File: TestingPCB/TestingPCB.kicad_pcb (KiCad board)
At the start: 2 copper layers, 15 parts, among them J1 Conn_01x04, J2 USB_C_Receptacle_USB2.0_14P, J3 Conn_01x08, U1 SC0915, U2 CP2102N-Axx-xQFN24, U3 USBLC6-2P6

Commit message: v1 of PCB
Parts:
- added H1: MountingHole, MountingHole:MountingHole_3.2mm_M3_ISO7380_Pad_TopBottom, F.Cu at (95.0, 70.0)
- added H2: MountingHole, MountingHole:MountingHole_3.2mm_M3_ISO7380_Pad_TopBottom, F.Cu at (175.0, 70.0)
- added H3: MountingHole, MountingHole:MountingHole_3.2mm_M3_ISO7380_Pad_TopBottom, F.Cu at (95.0, 140.0)
- added H4: MountingHole, MountingHole:MountingHole_3.2mm_M3_ISO7380_Pad_TopBottom, F.Cu at (175.0, 140.0)
- moved J3 132.0 mm to (135.0, 137.5), turned to -90 degrees
- moved J1 112.0 mm to (160.0, 72.5), turned to 90 degrees
- moved R3 92.8 mm to (108.0, 113.5), turned to 90 degrees
- moved R4 87.4 mm to (103.0, 113.5), turned to -90 degrees
- moved C1 86.2 mm to (104.5, 104.5), turned to -90 degrees
- moved C2 84.7 mm to (107.5, 104.5), turned to -90 degrees
- moved R5 82.0 mm to (111.5, 104.5), turned to 90 degrees
- moved R1 78.5 mm to (116.0, 82.5), turned to 90 degrees
- moved C3 74.0 mm to (99.5, 100.0), turned to 180 degrees
- moved U2 70.3 mm to (108.2, 98.6)
- moved C4 68.8 mm to (99.5, 97.5), turned to 180 degrees
- moved R2 67.5 mm to (103.5, 82.5), turned to 90 degrees
- moved U1 65.3 mm to (135.0, 92.5)
- moved U3 63.1 mm to (109.5, 82.3), turned to -90 degrees
- moved J2 49.5 mm to (110.0, 69.5), turned to 180 degrees
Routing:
- net /3.3V: track 0.00 -> 111.3 mm, vias 0 -> 3
- net /USB 5V: track 0.00 -> 75.9 mm, vias 0 -> 6
- net /D7: track 0.00 -> 63.3 mm, vias 0 -> 2
- net /D6: track 0.00 -> 55.1 mm, vias 0 -> 2
- net /D5: track 0.00 -> 50.8 mm, vias 0 -> 2
- net /D4: track 0.00 -> 45.8 mm, vias 0 -> 2
- net /D3: track 0.00 -> 41.6 mm, vias 0 -> 2
- net /RX: track 0.00 -> 37.5 mm, vias 0 -> 2
- net /D2: track 0.00 -> 36.7 mm, vias 0 -> 2
- net /TX: track 0.00 -> 36.0 mm
- net /5V: track 0.00 -> 32.3 mm
- net /D1: track 0.00 -> 30.9 mm, vias 0 -> 2
- net /D0: track 0.00 -> 27.1 mm
- net /D_N: track 0.00 -> 21.9 mm, vias 0 -> 2
- net /D_P: track 0.00 -> 18.5 mm
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- added copper zone on B.Cu, net /GND
- added copper zone on F.Cu, net /GND
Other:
- board outline added: 90 x 80 mm
- board text added: "5V"
- board text added: "ARM vs RISC-V Thesis Board"
- board text added: "By Robbie Leslie"
- board text added: "D0"
- board text added: "D1"
- board text added: "D2"
- board text added: "D3"
- board text added: "D4"
- board text added: "D5"
- board text added: "D6"
- board text added: "D7"
- board text added: "GND"
- board text added: "Lafayette College Electrical and Computer Engineering"
- board text added: "v1.0"

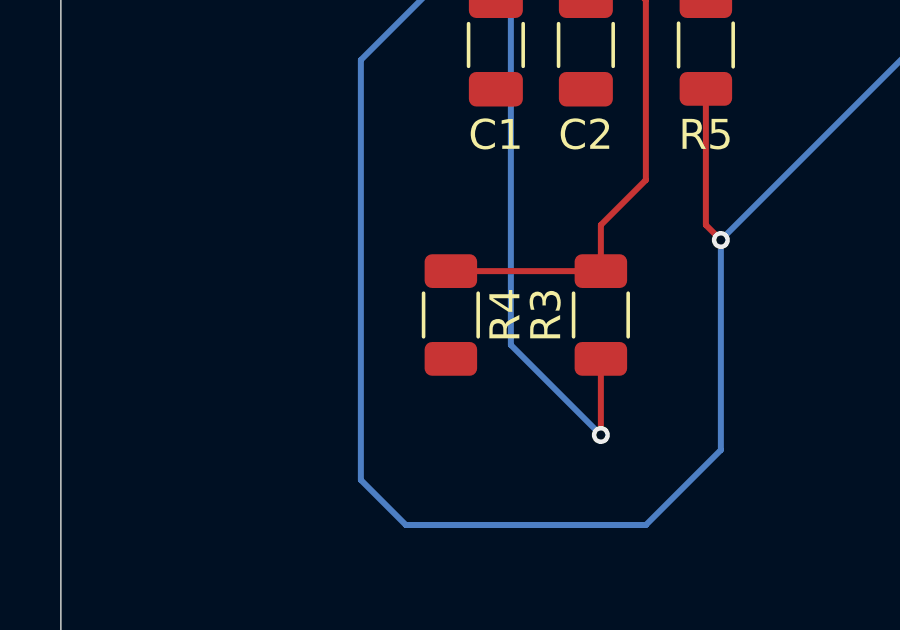
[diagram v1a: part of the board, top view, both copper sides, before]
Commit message: Updated silkscreen
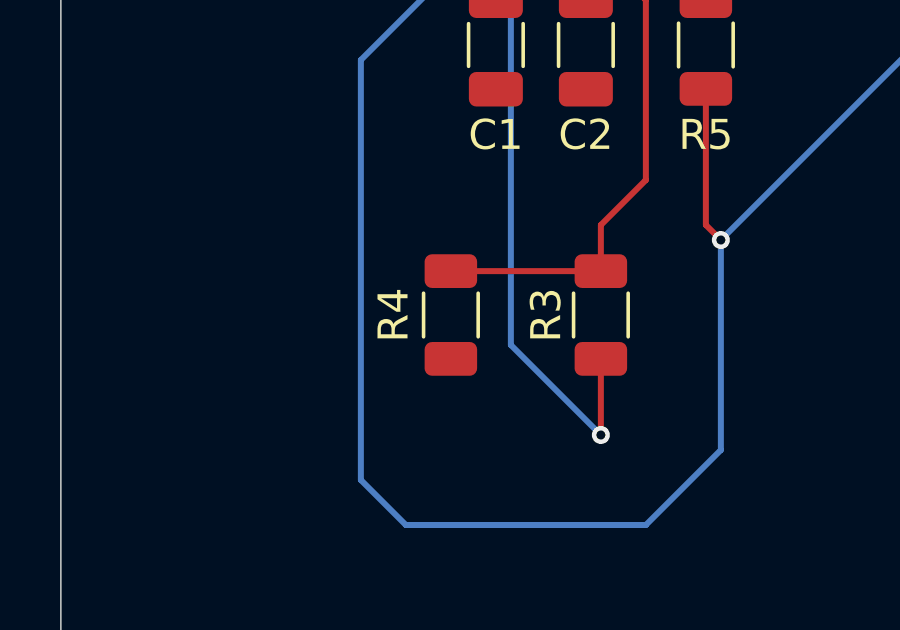
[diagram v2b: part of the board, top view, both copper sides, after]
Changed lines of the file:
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@@
 			(size 3.6 3.6)
 			(drill 3.2)
-			(layers "*.Cu" "*.Mask")
+			(layers "*.Cu" "*.Mask" "In1.Cu" "In2.Cu" "In3.Cu" "In4.Cu" "In5.Cu" "In6.Cu"
+				"In7.Cu" "In8.Cu" "In9.Cu" "In10.Cu" "In11.Cu" "In12.Cu" "In13.Cu" "In14.Cu"
+				"In15.Cu" "In16.Cu" "In17.Cu" "In18.Cu" "In19.Cu" "In20.Cu" "In21.Cu"
+				"In22.Cu" "In23.Cu" "In24.Cu" "In25.Cu" "In26.Cu" "In27.Cu" "In28.Cu"
+				"In29.Cu" "In30.Cu"
+			)
 			(remove_unused_layers no)
 		)
@@
 			(size 3.6 3.6)
 			(drill 3.2)
-			(layers "*.Cu" "*.Mask")
+			(layers "*.Cu" "*.Mask" "In1.Cu" "In2.Cu" "In3.Cu" "In4.Cu" "In5.Cu" "In6.Cu"
+				"In7.Cu" "In8.Cu" "In9.Cu" "In10.Cu" "In11.Cu" "In12.Cu" "In13.Cu" "In14.Cu"
+				"In15.Cu" "In16.Cu" "In17.Cu" "In18.Cu" "In19.Cu" "In20.Cu" "In21.Cu"
+				"In22.Cu" "In23.Cu" "In24.Cu" "In25.Cu" "In26.Cu" "In27.Cu" "In28.Cu"
+				"In29.Cu" "In30.Cu"
+			)
 			(remove_unused_layers no)
 		)
@@
 		(tags "resistor")
 		(property "Reference" "R4"
-			(at 0 -1.82 90)
+			(at 0 1.908 90)
 			(layer "F.SilkS")
 			(effects
@@
 		)
 		(fp_text user "${REFERENCE}"
-			(at -0.48 0 360)
+			(at -0.48 0 0)
 			(layer "F.Fab")
 			(effects
@@
 		(tags "capacitor")
 		(property "Reference" "C3"
-			(at 3.5 0 360)
+			(at 3.5 0 0)
 			(layer "F.SilkS")
 			(effects
@@
 		)
 		(property "Value" "4.7uF"
-			(at 0 1.85 360)
+			(at 0 1.85 0)
 			(layer "F.Fab")
 			(effects
@@
 		)
 		(fp_text user "${REFERENCE}"
-			(at 0 0 360)
+			(at 0 0 0)
 			(layer "F.Fab")
 			(effects
@@
 		)
 		(fp_text user "${REFERENCE}"
-			(at -0.48 0 360)
+			(at -0.48 0 0)
 			(layer "F.Fab")
 			(effects
@@
 		(tags "capacitor")
 		(property "Reference" "C4"
-			(at 3.5 0 360)
+			(at 3.5 0 0)
 			(layer "F.SilkS")
 			(effects
@@
 		)
 		(property "Value" "0.1uF"
-			(at 0 1.85 360)
+			(at 0 1.85 0)
 			(layer "F.Fab")
 			(effects
@@
 		)
 		(fp_text user "${REFERENCE}"
-			(at 0 0 360)
+			(at 0 0 0)
 			(layer "F.Fab")
 			(effects
@@
 			(size 0.65 0.65)
 			(drill 0.65)
-			(layers "*.Cu" "*.Mask")
+			(layers "*.Cu" "*.Mask" "In1.Cu" "In2.Cu" "In3.Cu" "In4.Cu" "In5.Cu" "In6.Cu"
+				"In7.Cu" "In8.Cu" "In9.Cu" "In10.Cu" "In11.Cu" "In12.Cu" "In13.Cu" "In14.Cu"
+				"In15.Cu" "In16.Cu" "In17.Cu" "In18.Cu" "In19.Cu" "In20.Cu" "In21.Cu"
+				"In22.Cu" "In23.Cu" "In24.Cu" "In25.Cu" "In26.Cu" "In27.Cu" "In28.Cu"
+				"In29.Cu" "In30.Cu"
+			)
 		)
 		(pad "" np_thru_hole circle
@@
 			(size 0.65 0.65)
 			(drill 0.65)
-			(layers "*.Cu" "*.Mask")
+			(layers "*.Cu" "*.Mask" "In1.Cu" "In2.Cu" "In3.Cu" "In4.Cu" "In5.Cu" "In6.Cu"
+				"In7.Cu" "In8.Cu" "In9.Cu" "In10.Cu" "In11.Cu" "In12.Cu" "In13.Cu" "In14.Cu"
+				"In15.Cu" "In16.Cu" "In17.Cu" "In18.Cu" "In19.Cu" "In20.Cu" "In21.Cu"
+				"In22.Cu" "In23.Cu" "In24.Cu" "In25.Cu" "In26.Cu" "In27.Cu" "In28.Cu"
+				"In29.Cu" "In30.Cu"
+			)
 		)
 		(pad "A1" smd roundrect
@@
 			(drill oval 0.6 1.7)
 			(property pad_prop_heatsink)
-			(layers "*.Cu" "*.Mask" "F.Paste")
+			(layers "*.Cu" "*.Mask" "In1.Cu" "In2.Cu" "In3.Cu" "In4.Cu" "In5.Cu" "In6.Cu"
+				"In7.Cu" "In8.Cu" "In9.Cu" "In10.Cu" "In11.Cu" "In12.Cu" "In13.Cu" "In14.Cu"
+				"In15.Cu" "In16.Cu" "In17.Cu" "In18.Cu" "In19.Cu" "In20.Cu" "In21.Cu"
+				"In22.Cu" "In23.Cu" "In24.Cu" "In25.Cu" "In26.Cu" "In27.Cu" "In28.Cu"
+				"In29.Cu" "In30.Cu" "F.Paste"
+			)
 			(remove_unused_layers no)
 			(net 10 "unconnected-(J2-SHIELD-PadS1)")
@@
 			(drill oval 0.6 1.4)
 			(property pad_prop_heatsink)
-			(layers "*.Cu" "*.Mask" "F.Paste")
+			(layers "*.Cu" "*.Mask" "In1.Cu" "In2.Cu" "In3.Cu" "In4.Cu" "In5.Cu" "In6.Cu"
+				"In7.Cu" "In8.Cu" "In9.Cu" "In10.Cu" "In11.Cu" "In12.Cu" "In13.Cu" "In14.Cu"
+				"In15.Cu" "In16.Cu" "In17.Cu" "In18.Cu" "In19.Cu" "In20.Cu" "In21.Cu"
+				"In22.Cu" "In23.Cu" "In24.Cu" "In25.Cu" "In26.Cu" "In27.Cu" "In28.Cu"
+				"In29.Cu" "In30.Cu" "F.Paste"
+			)
 			(remove_unused_layers no)
 			(net 10 "unconnected-(J2-SHIELD-PadS1)")
@@
 			(drill oval 0.6 1.7)
 			(property pad_prop_heatsink)
-			(layers "*.Cu" "*.Mask" "F.Paste")
+			(layers "*.Cu" "*.Mask" "In1.Cu" "In2.Cu" "In3.Cu" "In4.Cu" "In5.Cu" "In6.Cu"
+				"In7.Cu" "In8.Cu" "In9.Cu" "In10.Cu" "In11.Cu" "In12.Cu" "In13.Cu" "In14.Cu"
+				"In15.Cu" "In16.Cu" "In17.Cu" "In18.Cu" "In19.Cu" "In20.Cu" "In21.Cu"
+				"In22.Cu" "In23.Cu" "In24.Cu" "In25.Cu" "In26.Cu" "In27.Cu" "In28.Cu"
+				"In29.Cu" "In30.Cu" "F.Paste"
+			)
 			(remove_unused_layers no)
 			(net 10 "unconnected-(J2-SHIELD-PadS1)")
@@
 			(drill oval 0.6 1.4)
 			(property pad_prop_heatsink)
-			(layers "*.Cu" "*.Mask" "F.Paste")
+			(layers "*.Cu" "*.Mask" "In1.Cu" "In2.Cu" "In3.Cu" "In4.Cu" "In5.Cu" "In6.Cu"
+				"In7.Cu" "In8.Cu" "In9.Cu" "In10.Cu" "In11.Cu" "In12.Cu" "In13.Cu" "In14.Cu"
+				"In15.Cu" "In16.Cu" "In17.Cu" "In18.Cu" "In19.Cu" "In20.Cu" "In21.Cu"
+				"In22.Cu" "In23.Cu" "In24.Cu" "In25.Cu" "In26.Cu" "In27.Cu" "In28.Cu"
+				"In29.Cu" "In30.Cu" "F.Paste"
+			)
 			(remove_unused_layers no)
 			(net 10 "unconnected-(J2-SHIELD-PadS1)")
@@
 			(size 3.6 3.6)
 			(drill 3.2)
-			(layers "*.Cu" "*.Mask")
+			(layers "*.Cu" "*.Mask" "In1.Cu" "In2.Cu" "In3.Cu" "In4.Cu" "In5.Cu" "In6.Cu"
+				"In7.Cu" "In8.Cu" "In9.Cu" "In10.Cu" "In11.Cu" "In12.Cu" "In13.Cu" "In14.Cu"
+				"In15.Cu" "In16.Cu" "In17.Cu" "In18.Cu" "In19.Cu" "In20.Cu" "In21.Cu"
+				"In22.Cu" "In23.Cu" "In24.Cu" "In25.Cu" "In26.Cu" "In27.Cu" "In28.Cu"
+				"In29.Cu" "In30.Cu"
+			)
 			(remove_unused_layers no)
 		)
@@
 		)
 		(fp_text user "${REFERENCE}"
-			(at 0 0 360)
+			(at 0 0 0)
 			(layer "F.Fab")
 			(effects
@@
 			(size 3.6 3.6)
 			(drill 3.2)
-			(layers "*.Cu" "*.Mask")
+			(layers "*.Cu" "*.Mask" "In1.Cu" "In2.Cu" "In3.Cu" "In4.Cu" "In5.Cu" "In6.Cu"
+				"In7.Cu" "In8.Cu" "In9.Cu" "In10.Cu" "In11.Cu" "In12.Cu" "In13.Cu" "In14.Cu"
+				"In15.Cu" "In16.Cu" "In17.Cu" "In18.Cu" "In19.Cu" "In20.Cu" "In21.Cu"
+				"In22.Cu" "In23.Cu" "In24.Cu" "In25.Cu" "In26.Cu" "In27.Cu" "In28.Cu"
+				"In29.Cu" "In30.Cu"
+			)
 			(remove_unused_layers no)
 		)
@@
 		(net 2)
 		(net_name "/GND")
-		(layers "F&B.Cu")
+		(layers "F.Cu" "B.Cu")
 		(hatch edge 0.5)
 		(connect_pads

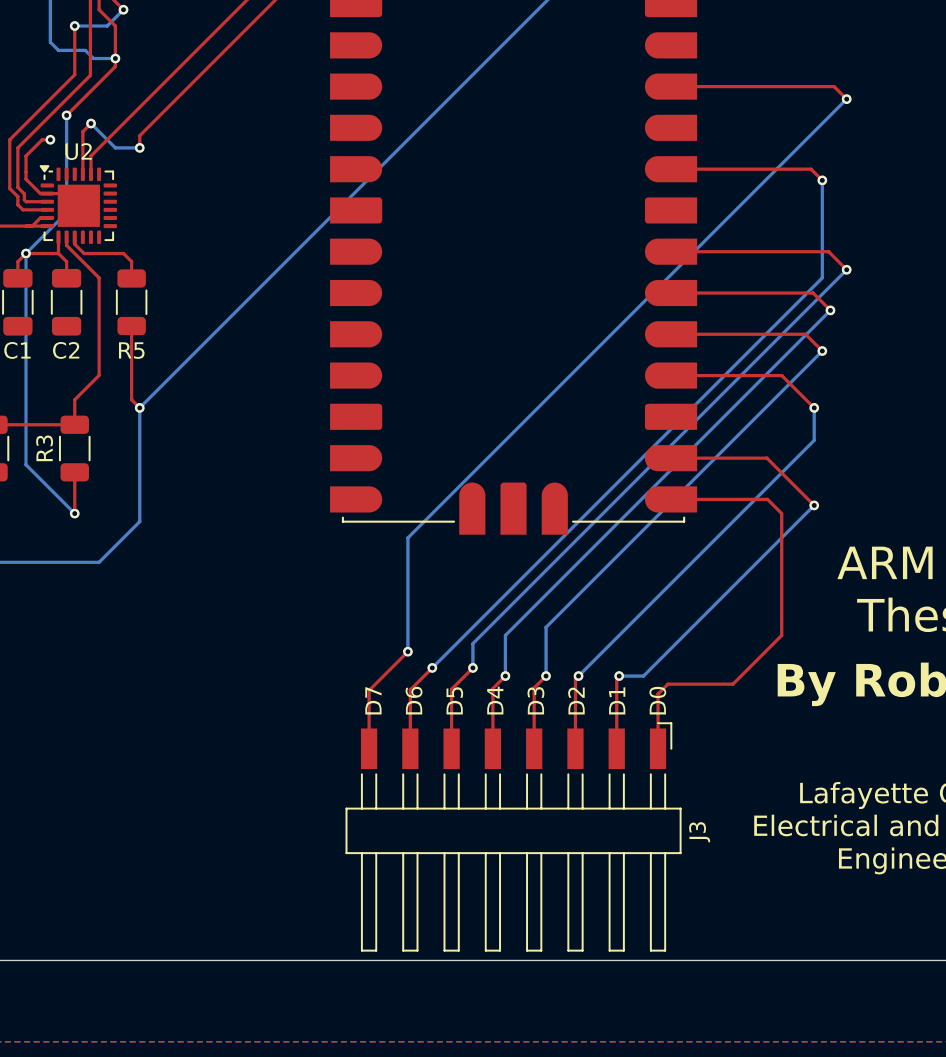
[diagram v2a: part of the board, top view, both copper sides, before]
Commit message: Updated PCB with 10 pin logic connector
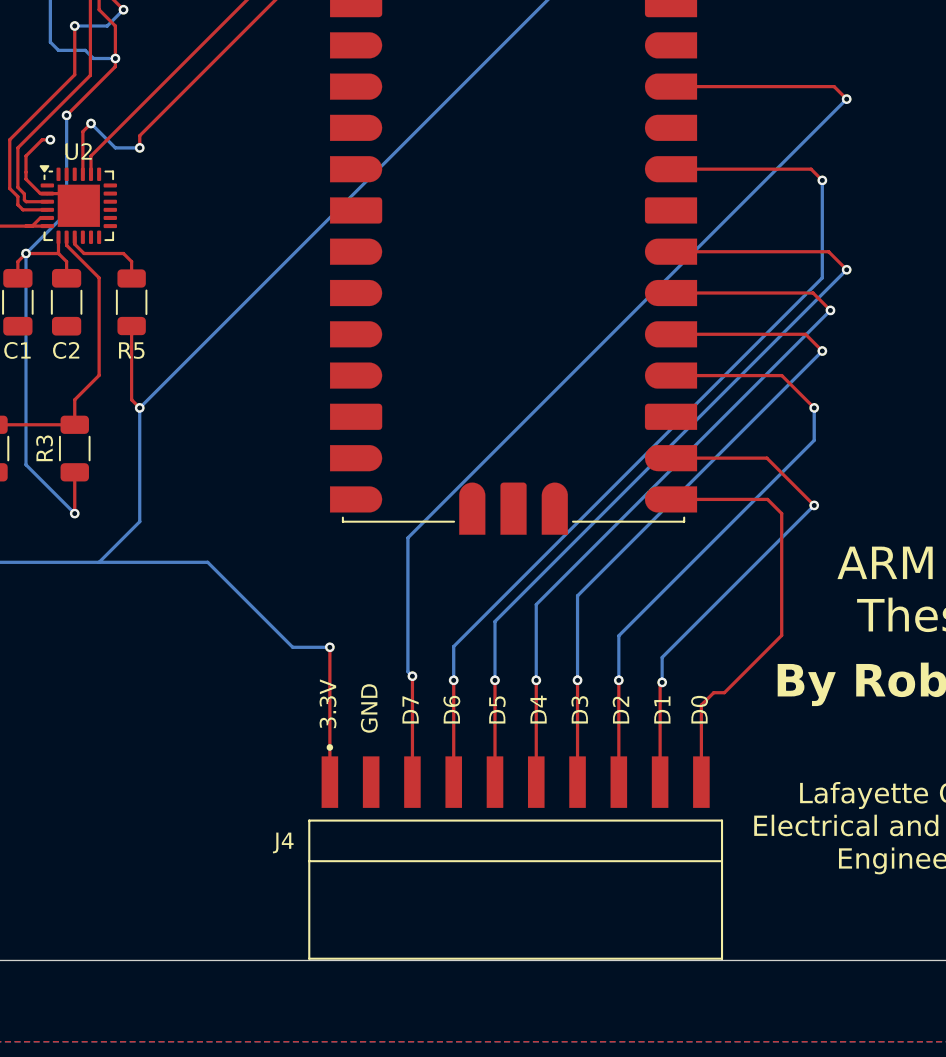
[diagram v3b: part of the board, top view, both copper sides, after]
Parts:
- removed J3: Conn_01x08, Connector_Harwin:Harwin_M20-89008xx_1x08_P2.54mm_Horizontal
- added J4: Conn_01x10, Footprints:HARWIN_M20-8891045, F.Cu at (135.1, 137.6)
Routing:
- net /3.3V: track 111.3 -> 136.0 mm, vias 3 -> 4
- net /D7: track 63.3 -> 64.5 mm
- net /D0: track 27.1 -> 26.1 mm
- net /D3: track 41.6 -> 42.5 mm
- net /D5: track 50.8 -> 51.8 mm
- net /D6: track 55.1 -> 56.0 mm
- net /D4: track 45.8 -> 46.8 mm
- net /D2: track 36.7 -> 37.6 mm
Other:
- board text added: "3.3V"

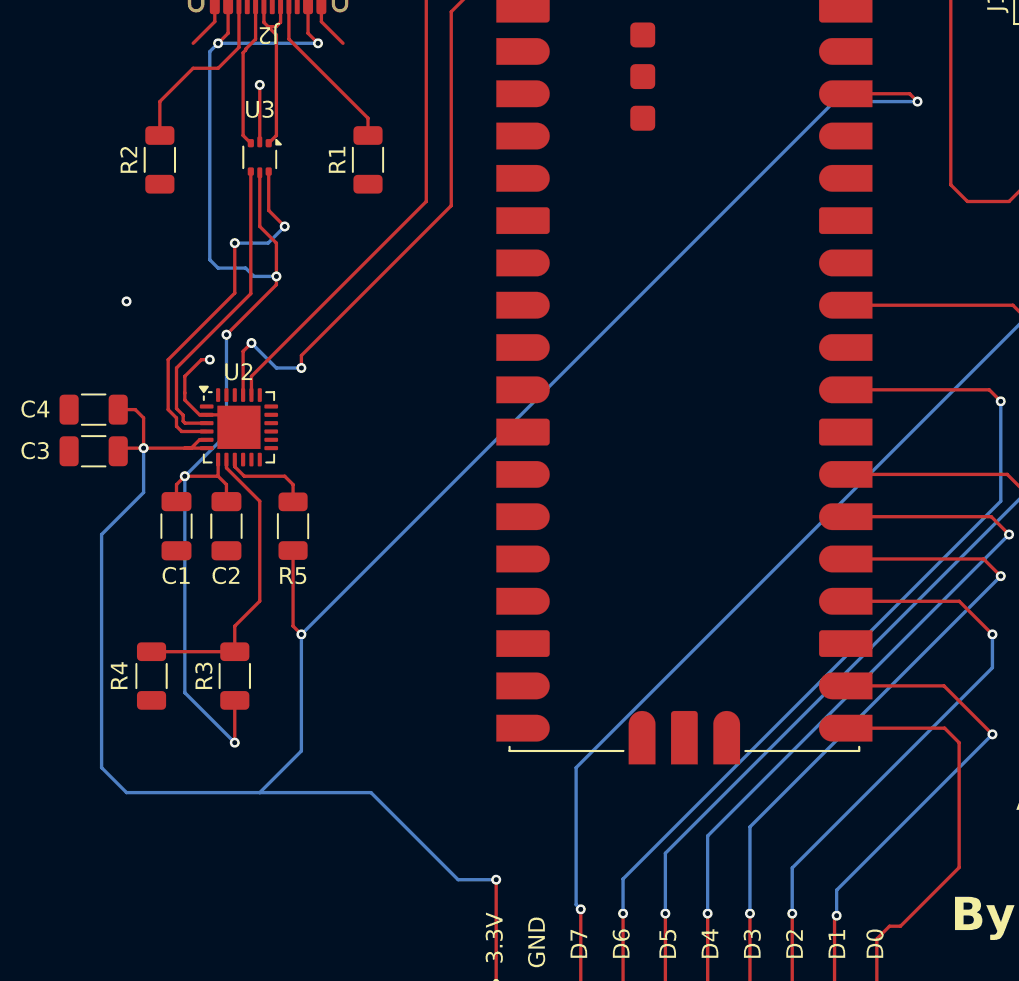
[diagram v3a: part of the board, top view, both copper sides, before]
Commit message: Updated to use the 20 pin package and fixed power for CP2102N
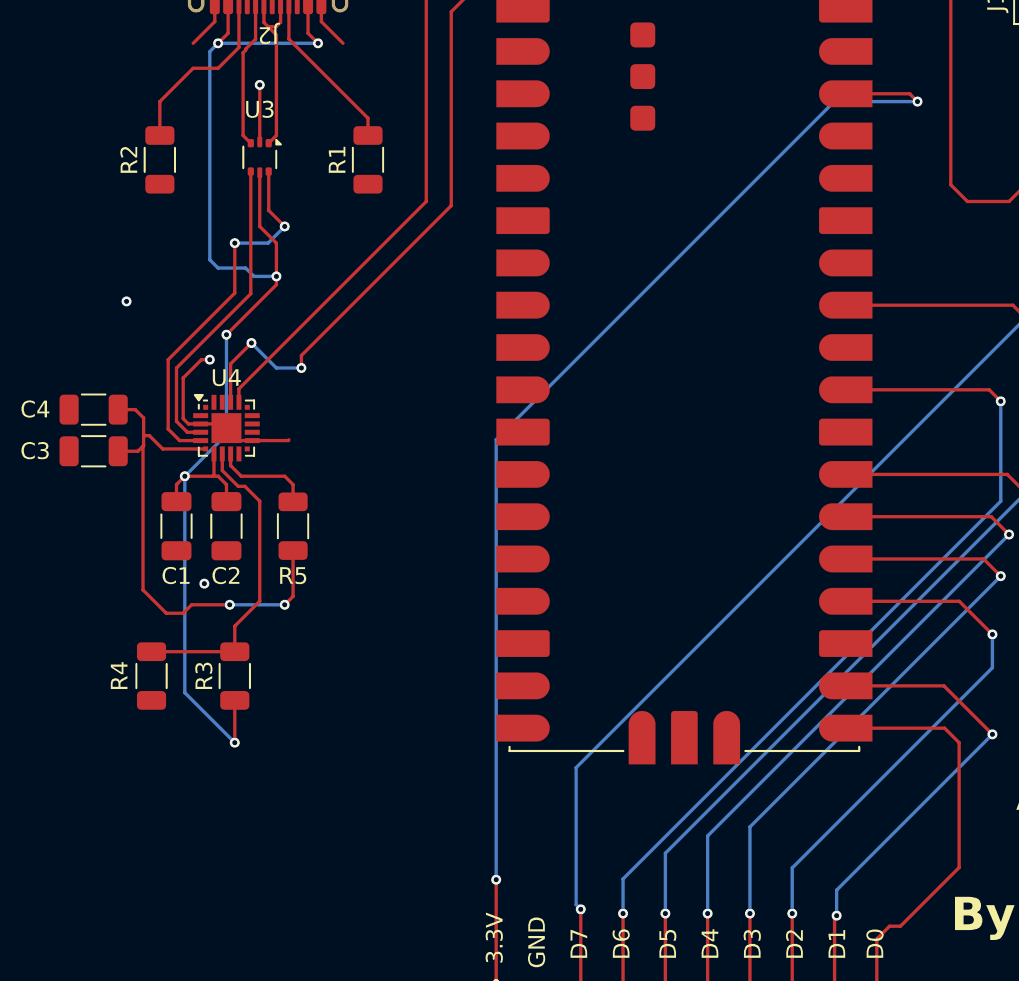
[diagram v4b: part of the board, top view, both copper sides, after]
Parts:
- removed U2: CP2102N-Axx-xQFN24, Package_DFN_QFN:QFN-24-1EP_4x4mm_P0.5mm_EP2.6x2.6mm
- added U4: CP2102N-Axx-xQFN20, Package_DFN_QFN:SiliconLabs_QFN-20-1EP_3x3mm_P0.5mm_EP1.8x1.8mm, F.Cu at (107.5, 98.6)
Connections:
- C3 pad 1: /3.3V -> /VDD
- C4 pad 1: /3.3V -> /VDD
- R5 pad 1: /3.3V -> /VDD
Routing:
- net /3.3V: track 136.0 -> 72.9 mm, vias 4 -> 2
- net /VDD: track 0.00 -> 30.8 mm, vias 0 -> 2
- net /GND: track 16.4 -> 20.6 mm, vias 3 -> 4
- net /TX: track 36.0 -> 36.7 mm
- net /RX: track 37.5 -> 38.2 mm
- net Net-(U4-VBUS): track 18.0 -> 18.7 mm
- net Net-(U4-~{RST}): track 5.41 -> 5.96 mm
